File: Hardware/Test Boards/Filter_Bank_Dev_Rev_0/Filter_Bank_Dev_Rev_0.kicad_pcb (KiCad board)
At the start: 2 copper layers, 50 x 50 mm, 24 parts, among them J1 USB_B_Micro, J2 RF IN, J3 RF OUT, SW1 KAE02LGGR, U1 PE42440, U2 74AHC1G04, U3 AMS1117-3.3, U4 PE42440

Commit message: Filter Bank layout finished
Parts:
- added G***: LOGO, VNA_Footprints:OSHW_Logo_3.6x3.6_F.Mask, F.Cu at (126.2, 86.8)
- added REF**: Board Title, VNA_Footprints:BoardTitle, F.Cu at (118.7, 45.7)
- added REF**: 4LayerCheck, VNA_Footprints:4LayerCheck, F.Cu at (132.7, 87.0)
- added REF**: Josh Details, VNA_Footprints:JoshDetails, B.Cu at (131.2, 82.5)
- FL3: value Filter_LFCN-400D+ -> Filter_LFCN-1000+
- FL4: value Filter_LFCN-1000+ -> Filter_LFCN-400D+
- U1, U4: footprint Package_DFN_QFN:QFN-16-1EP_3x3mm_P0.5mm_EP2.7x2.7mm_ThermalVias -> VNA_Footprints:QFN-16-1EP_3x3mm_P0.5mm_EP2.7x2.7mm_ThermalVias
- moved U2 65.9 mm to (108.5, 72.5)
- moved C1 57.9 mm to (109.0, 65.0), turned to 180 degrees
- moved R1 56.4 mm to (108.6, 75.3), turned to 180 degrees
- moved C3 49.6 mm to (125.2, 64.2), turned to 270 degrees
- moved R2 49.6 mm to (113.0, 75.2)
- moved J3 47.8 mm to (142.8, 65.0), turned to 0 degrees
- moved J2 47.8 mm to (97.2, 65.0), turned to 180 degrees
- moved C4 45.2 mm to (129.8, 57.5), turned to 270 degrees
- moved C6 37.0 mm to (131.4, 65.0), turned to 180 degrees
- moved U3 26.7 mm to (135.8, 56.1), turned to 180 degrees
- moved C5 21.1 mm to (114.8, 66.0), turned to 90 degrees
- moved FL4 19.5 mm to (120.2, 58.2)
- moved FL1 17.2 mm to (120.2, 72.2)
- moved C2 15.5 mm to (139.9, 51.5)
- moved FL2 8.25 mm to (120.2, 68.2)
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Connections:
- FL1 pad 3: /SW_2_RF_1 -> /SW_2_RF_3
- FL2 pad 3: /SW_2_RF_2 -> /SW_2_RF_4
- FL3 pad 1: /SW_1_RF_3 -> /SW_1_RF_4
- FL3 pad 3: /SW_2_RF_3 -> /SW_2_RF_2
- FL4 pad 1: /SW_1_RF_4 -> /SW_1_RF_3
- FL4 pad 3: /SW_2_RF_4 -> /SW_2_RF_1
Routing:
- net GND: track 0.00 -> 30.2 mm, vias 0 -> 339
- net /SW_1_CTRL_2: track 0.00 -> 28.2 mm, vias 0 -> 3
- net +5V: track 0.00 -> 24.2 mm
- net /SW_1_CTRL_1: track 0.00 -> 23.2 mm, vias 0 -> 2
- net +3V3: track 0.00 -> 22.8 mm, vias 0 -> 8
- net /SW_2_CTRL_1: track 0.00 -> 20.8 mm, vias 0 -> 2
- net Net-(C1-Pad2): track 0.00 -> 11.5 mm
- net Net-(C6-Pad1): track 0.00 -> 11.1 mm
- net /SW_1_RF_1: track 0.00 -> 10.1 mm
- net /SW_2_RF_3: track 0.00 -> 9.97 mm
- net /SW_2_RF_1: track 0.00 -> 9.94 mm
- net /SW_1_RF_3: track 0.00 -> 9.73 mm
- net /SW_1_RF_2: track 0.00 -> 7.41 mm
- net /SW_2_RF_2: track 0.00 -> 7.19 mm
- net /SW_2_RF_4: track 0.00 -> 7.17 mm
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- added copper zone on F.Cu, net +3V3
- added copper zone on In2.Cu, net +3V3
- added copper zone on B.Cu, net GND
- added copper zone on F.Cu, net GND
- added copper zone on In1.Cu, net GND
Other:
- copper layers 2 -> 4
- net class Default: clearance 0.2 -> 0.1
- net class RF added: clearance 0.1, trace_width 0.31, via_dia 0.45, via_drill 0.2
- rule trace_clearance: 0.2 -> 0.1
- rule trace_min: 0.2 -> 0.127
- rule via_min_drill: 0.3 -> 0.2
- rule via_min_size: 0.4 -> 0.45

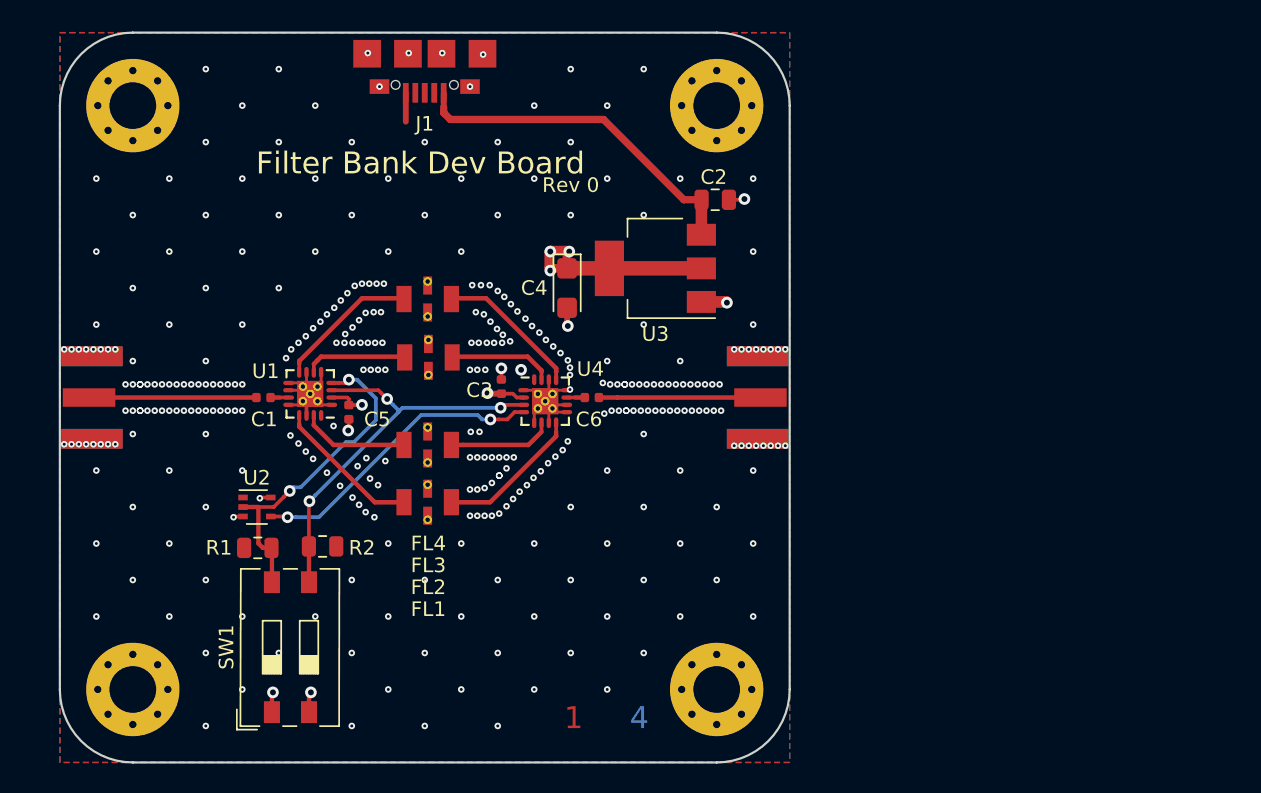
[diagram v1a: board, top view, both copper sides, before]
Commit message: Changed coupler to 4 layer board, turned gerbers into panel, made BOM spreadsheet.
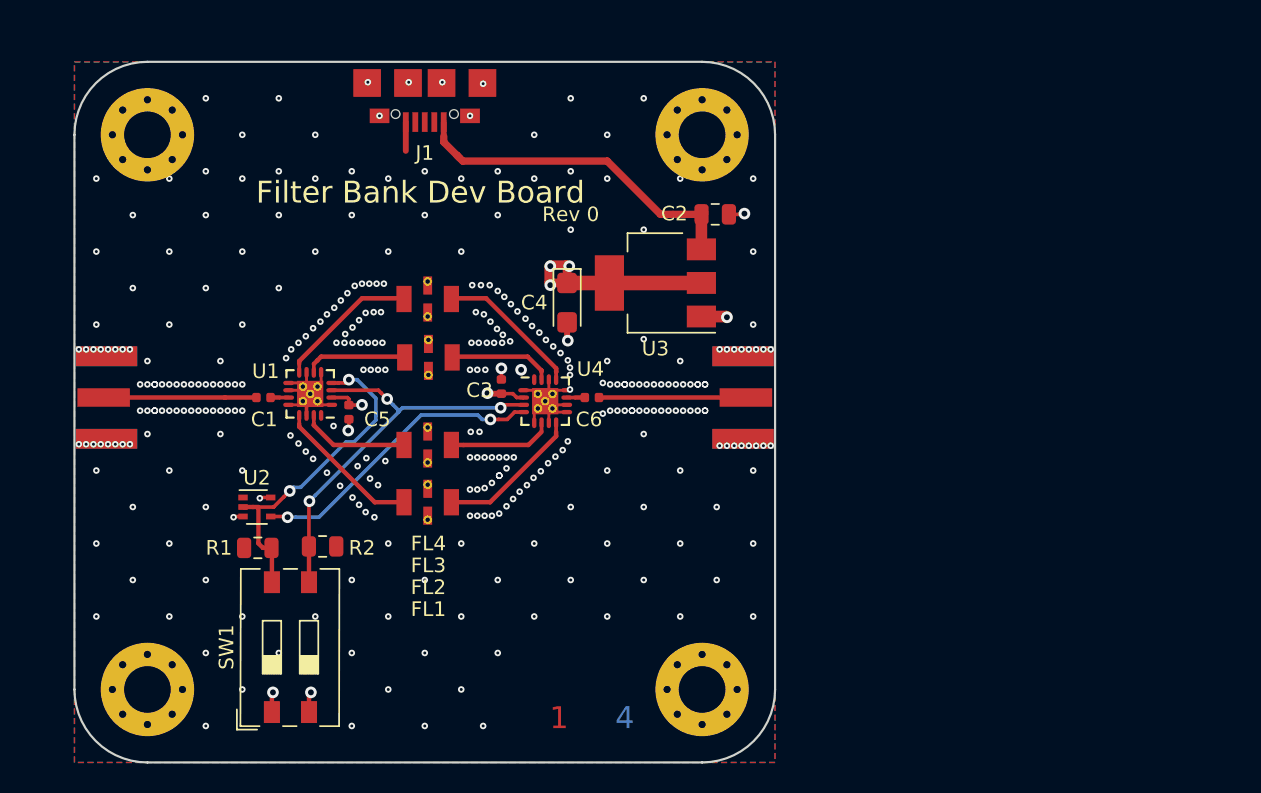
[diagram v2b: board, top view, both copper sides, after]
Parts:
- moved H2 2.24 mm to (139.0, 47.0)
- moved H3 2.24 mm to (101.0, 47.0)
- moved J1 2.00 mm to (120.0, 42.0)
- moved REF** 2.00 mm to (118.7, 47.7)
- moved C2 1.00 mm to (139.9, 52.5)
- moved C4 1.00 mm to (129.8, 58.5)
- moved H1 1.00 mm to (101.0, 85.0)
- moved H4 1.00 mm to (139.0, 85.0)
- moved J2 1.00 mm to (98.2, 65.0)
- moved J3 1.00 mm to (141.8, 65.0)
- moved REF** 1.00 mm to (131.7, 87.0)
- moved REF** 1.00 mm to (130.2, 82.5)
- moved U3 1.00 mm to (135.8, 57.1)
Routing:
- net Net-(C6-Pad1): track 11.1 -> 10.1 mm
- net Net-(C1-Pad2): track 11.5 -> 10.5 mm
- net GND: track 30.2 -> 30.1 mm, vias 339 -> 330
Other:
- board size 50 x 50 mm -> 48 x 48 mm

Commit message: Finalised Gerbers to be sent off to the fab
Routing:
- net GND: vias 330 -> 328
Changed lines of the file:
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@@
     (thickness 1.6)
     (drawings 8)
-    (tracks 517)
+    (tracks 512)
     (zones 0)
     (modules 28)
@@
   (via (at 129.8 62.45) (size 0.45) (drill 0.2) (layers F.Cu B.Cu) (net 4))
   (via (at 127.35 60.1) (size 0.45) (drill 0.2) (layers F.Cu B.Cu) (net 4))
-  (via (at 129.95 64.45) (size 0.45) (drill 0.2) (layers F.Cu B.Cu) (net 4))
   (via (at 123.25 57.3) (size 0.45) (drill 0.2) (layers F.Cu B.Cu) (net 4))
   (via (at 123.85 57.3) (size 0.45) (drill 0.2) (layers F.Cu B.Cu) (net 4))
@@
   (via (at 117.5 50) (size 0.45) (drill 0.2) (layers F.Cu B.Cu) (net 4))
   (via (at 112.5 50) (size 0.45) (drill 0.2) (layers F.Cu B.Cu) (net 4))
-  (via (at 102.5 50) (size 0.45) (drill 0.2) (layers F.Cu B.Cu) (net 4))
   (via (at 97.5 55) (size 0.45) (drill 0.2) (layers F.Cu B.Cu) (net 4))
   (via (at 97.5 50) (size 0.45) (drill 0.2) (layers F.Cu B.Cu) (net 4))
@@
   (via (at 142.5 60) (size 0.45) (drill 0.2) (layers F.Cu B.Cu) (net 4))
   (via (at 142.5 55) (size 0.45) (drill 0.2) (layers F.Cu B.Cu) (net 4))
-  (via (at 137.5 50) (size 0.45) (drill 0.2) (layers F.Cu B.Cu) (net 4))
   (via (at 142.5 50) (size 0.45) (drill 0.2) (layers F.Cu B.Cu) (net 4))
   (via (at 107 64.1) (size 0.45) (drill 0.2) (layers F.Cu B.Cu) (net 4))
@@
   (via (at 107 65.9) (size 0.45) (drill 0.2) (layers F.Cu B.Cu) (net 4))
   (via (at 133.2 65.9) (size 0.45) (drill 0.2) (layers F.Cu B.Cu) (net 4))
+  (via (at 117.2 67.7) (size 0.45) (drill 0.2) (layers F.Cu B.Cu) (net 4))
   (segment (start 129.75 57.15) (end 132.65 57.15) (width 1) (layer F.Cu) (net 5))
   (segment (start 138.95 57.15) (end 132.65 57.15) (width 1) (layer F.Cu) (net 5))
@@
   (segment (start 109.53 75.33) (end 109.5 75.3) (width 0.3) (layer F.Cu) (net 19))
   (segment (start 109.53 77.65) (end 109.53 75.33) (width 0.3) (layer F.Cu) (net 19))
-  (segment (start 108.175 72.5) (end 107.55 72.5) (width 0.3) (layer F.Cu) (net 19))
-  (segment (start 108.255 72.5) (end 108.175 72.5) (width 0.3) (layer F.Cu) (net 19))
-  (segment (start 108.6 72.5) (end 108.255 72.5) (width 0.3) (layer F.Cu) (net 19))
-  (segment (start 108.6 74.9875) (end 108.6 72.5) (width 0.3) (layer F.Cu) (net 19))
-  (segment (start 109.5 75.3) (end 108.9125 75.3) (width 0.3) (layer F.Cu) (net 19))
-  (segment (start 108.9125 75.3) (end 108.6 74.9875) (width 0.3) (layer F.Cu) (net 19))
   (segment (start 113.625 64) (end 114.1 64) (width 0.25) (layer F.Cu) (net 19))
   (via (at 114.8 63.775) (size 0.8) (drill 0.4) (layers F.Cu B.Cu) (net 19))
   (segment (start 114.1 64) (end 114.575 64) (width 0.25) (layer F.Cu) (net 19))
   (segment (start 114.575 64) (end 114.8 63.775) (width 0.25) (layer F.Cu) (net 19))
-  (segment (start 110.350001 71.799999) (end 110.75 71.4) (width 0.25) (layer F.Cu) (net 19))
-  (segment (start 108.255 72.5) (end 109.65 72.5) (width 0.25) (layer F.Cu) (net 19))
-  (segment (start 109.65 72.5) (end 110.350001 71.799999) (width 0.25) (layer F.Cu) (net 19))
   (via (at 110.75 71.4) (size 0.8) (drill 0.4) (layers F.Cu B.Cu) (net 19))
   (segment (start 114.8 63.775) (end 115.365685 63.775) (width 0.25) (layer B.Cu) (net 19))
@@
   (segment (start 110.75 71.4) (end 111 71.15) (width 0.25) (layer B.Cu) (net 19))
   (segment (start 111 71.15) (end 111.5 71.15) (width 0.25) (layer B.Cu) (net 19))
+  (segment (start 108.6 75.1) (end 108.6 72.6) (width 0.25) (layer F.Cu) (net 19))
+  (segment (start 108.255 72.5) (end 107.55 72.5) (width 0.25) (layer F.Cu) (net 19))
+  (segment (start 110.75 71.4) (end 109.65 72.5) (width 0.25) (layer F.Cu) (net 19))
+  (segment (start 109.65 72.5) (end 108.255 72.5) (width 0.25) (layer F.Cu) (net 19))
+  (segment (start 108.8 75.3) (end 109.5 75.3) (width 0.25) (layer F.Cu) (net 19))
+  (segment (start 108.6 75.1) (end 108.8 75.3) (width 0.25) (layer F.Cu) (net 19))
   (segment (start 112.07 75.2075) (end 112.0625 75.2) (width 0.3) (layer F.Cu) (net 20))
   (segment (start 112.07 77.65) (end 112.07 75.2075) (width 0.3) (layer F.Cu) (net 20))
